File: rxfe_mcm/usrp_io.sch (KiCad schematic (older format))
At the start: 17 parts, among them J201 DB15, U202 CONN_SMA, U203 74HC04_FULL, U204 CONN_SMA, U205 ADP7158, U206 CONN_SMA, U209 CONN_SMA

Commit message: added some notes/errata to the transmitter schematics
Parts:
- J201: PN (none) -> 609-1498-ND
- RP201, RP202, RP204: PN (none) -> TC164J-1.0KCT-ND
- U202, U204, U206, U209: PN (none) -> CONSMA002-L-ND
- U203: PN (none) -> 296-8208-1-ND
- U205: PN (none) -> ADP7158ACPZ-3.3-R7CT-ND
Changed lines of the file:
@@
 LIBS:adp7158
 LIBS:pe4312
+LIBS:rxfe_mcm-cache
 EELAYER 25 0
 EELAYER END
@@
 F 2 "footprints:DB15MC" H 1700 1750 50  0001 C CNN
 F 3 "" H 1700 1750 50  0000 C CNN
+F 4 "609-1498-ND" H 1700 1750 60  0001 C CNN "PN"
 	1    1700 1750
 	-1   0    0    -1
@@
 F 2 "footprints:SMA_rightangle" H 1750 6800 60  0001 C CNN
 F 3 "" H 1750 6800 60  0000 C CNN
+F 4 "CONSMA002-L-ND" H 1750 6800 60  0001 C CNN "PN"
 	1    1750 6800
 	-1   0    0    -1
@@
 F 2 "Resistors_SMD:R_Array_Concave_4x0603" H 3550 2150 50  0001 C CNN
 F 3 "" H 3550 2150 50  0000 C CNN
+F 4 "TC164J-1.0KCT-ND" H 3550 2150 60  0001 C CNN "PN"
 	1    3550 2150
 	1    0    0    1
@@
 F 2 "Resistors_SMD:R_Array_Concave_4x0603" H 3550 1000 50  0001 C CNN
 F 3 "" H 3550 1000 50  0000 C CNN
+F 4 "TC164J-1.0KCT-ND" H 3550 1000 60  0001 C CNN "PN"
 	1    3550 1000
 	1    0    0    1
@@
 F 2 "Housings_SSOP:TSSOP-14_4.4x5mm_Pitch0.65mm" H 8100 2300 60  0001 C CNN
 F 3 "" H 8100 2300 60  0000 C CNN
+F 4 "296-8208-1-ND" H 8100 2300 60  0001 C CNN "PN"
 	1    8100 2300
 	1    0    0    -1
@@
 $EndComp
 $Comp
-L GND #PWR03
+L GND #PWR01
 U 1 1 59826F34
 P 9000 1750
-F 0 "#PWR03" H 9000 1500 50  0001 C CNN
+F 0 "#PWR01" H 9000 1500 50  0001 C CNN
 F 1 "GND" H 9000 1600 50  0000 C CNN
 F 2 "" H 9000 1750 50  0000 C CNN
@@
 AMPB2_CTRL
 $Comp
-L GND #PWR04
+L GND #PWR02
 U 1 1 5982BDE0
 P 7550 2700
-F 0 "#PWR04" H 7550 2450 50  0001 C CNN
+F 0 "#PWR02" H 7550 2450 50  0001 C CNN
 F 1 "GND" H 7550 2550 50  0000 C CNN
 F 2 "" H 7550 2700 50  0000 C CNN
@@
 F 2 "Housings_DFN_QFN:DFN-10-1EP_3x3mm_Pitch0.5mm" H 8150 4550 60  0001 C CNN
 F 3 "" H 8150 4550 60  0001 C CNN
+F 4 "ADP7158ACPZ-3.3-R7CT-ND" H 8150 4550 60  0001 C CNN "PN"
 	1    8150 4550
 	1    0    0    -1
@@
 $EndComp
 $Comp
-L GND #PWR05
+L GND #PWR03
 U 1 1 598D7D01
 P 9400 1750
-F 0 "#PWR05" H 9400 1500 50  0001 C CNN
+F 0 "#PWR03" H 9400 1500 50  0001 C CNN
 F 1 "GND" H 9400 1600 50  0000 C CNN
 F 2 "" H 9400 1750 50  0000 C CNN
@@
 $EndComp
 $Comp
-L +3V3 #PWR06
+L +3V3 #PWR04
 U 1 1 598DD83D
 P 7000 4200
-F 0 "#PWR06" H 7000 4050 50  0001 C CNN
+F 0 "#PWR04" H 7000 4050 50  0001 C CNN
 F 1 "+3V3" H 7000 4340 50  0000 C CNN
 F 2 "" H 7000 4200 50  0000 C CNN
@@
 $EndComp
 $Comp
-L VPP #PWR07
+L VPP #PWR05
 U 1 1 59903DFA
 P 9700 4200
-F 0 "#PWR07" H 9700 4050 50  0001 C CNN
+F 0 "#PWR05" H 9700 4050 50  0001 C CNN
 F 1 "VPP" H 9700 4350 50  0000 C CNN
 F 2 "" H 9700 4200 50  0000 C CNN
@@
 $EndComp
 $Comp
-L GND #PWR08
+L GND #PWR06
 U 1 1 599045BA
 P 8900 5300
-F 0 "#PWR08" H 8900 5050 50  0001 C CNN
+F 0 "#PWR06" H 8900 5050 50  0001 C CNN
 F 1 "GND" H 8900 5150 50  0000 C CNN
 F 2 "" H 8900 5300 50  0000 C CNN
@@
 $EndComp
 $Comp
-L GND #PWR09
+L GND #PWR07
 U 1 1 59904683
 P 9300 5300
-F 0 "#PWR09" H 9300 5050 50  0001 C CNN
+F 0 "#PWR07" H 9300 5050 50  0001 C CNN
 F 1 "GND" H 9300 5150 50  0000 C CNN
 F 2 "" H 9300 5300 50  0000 C CNN
@@
 $EndComp
 $Comp
-L GND #PWR010
+L GND #PWR08
 U 1 1 599046FD
 P 9700 5300
-F 0 "#PWR010" H 9700 5050 50  0001 C CNN
+F 0 "#PWR08" H 9700 5050 50  0001 C CNN
 F 1 "GND" H 9700 5150 50  0000 C CNN
 F 2 "" H 9700 5300 50  0000 C CNN
@@
 $EndComp
 $Comp
-L GND #PWR011
+L GND #PWR09
 U 1 1 599050DD
 P 7300 5300
-F 0 "#PWR011" H 7300 5050 50  0001 C CNN
+F 0 "#PWR09" H 7300 5050 50  0001 C CNN
 F 1 "GND" H 7300 5150 50  0000 C CNN
 F 2 "" H 7300 5300 50  0000 C CNN
@@
 $EndComp
 $Comp
-L GND #PWR012
+L GND #PWR010
 U 1 1 5990515D
 P 7000 5300
-F 0 "#PWR012" H 7000 5050 50  0001 C CNN
+F 0 "#PWR010" H 7000 5050 50  0001 C CNN
 F 1 "GND" H 7000 5150 50  0000 C CNN
 F 2 "" H 7000 5300 50  0000 C CNN
@@
 $EndComp
 $Comp
-L GND #PWR013
+L GND #PWR011
 U 1 1 59905965
 P 8150 5300
-F 0 "#PWR013" H 8150 5050 50  0001 C CNN
+F 0 "#PWR011" H 8150 5050 50  0001 C CNN
 F 1 "GND" H 8150 5150 50  0000 C CNN
 F 2 "" H 8150 5300 50  0000 C CNN
@@
 $EndComp
 $Comp
-L VPP #PWR014
+L VPP #PWR012
 U 1 1 5990693F
 P 7500 5100
-F 0 "#PWR014" H 7500 4950 50  0001 C CNN
+F 0 "#PWR012" H 7500 4950 50  0001 C CNN
 F 1 "VPP" H 7500 5250 50  0000 C CNN
 F 2 "" H 7500 5100 50  0000 C CNN
@@
 $EndComp
 $Comp
-L +3V3 #PWR015
+L +3V3 #PWR013
 U 1 1 5991D035
 P 9000 1050
-F 0 "#PWR015" H 9000 900 50  0001 C CNN
+F 0 "#PWR013" H 9000 900 50  0001 C CNN
 F 1 "+3V3" H 9000 1190 50  0000 C CNN
 F 2 "" H 9000 1050 50  0000 C CNN
@@
 $EndComp
 $Comp
-L GND #PWR016
+L GND #PWR014
 U 1 1 5983E2EE
 P 1800 7450
-F 0 "#PWR016" H 1800 7200 50  0001 C CNN
+F 0 "#PWR014" H 1800 7200 50  0001 C CNN
 F 1 "GND" H 1800 7300 50  0000 C CNN
 F 2 "" H 1800 7450 50  0000 C CNN
@@
 F 2 "footprints:SMA_rightangle" H 1750 5600 60  0001 C CNN
 F 3 "" H 1750 5600 60  0000 C CNN
+F 4 "CONSMA002-L-ND" H 1750 5600 60  0001 C CNN "PN"
 	1    1750 5600
 	-1   0    0    -1
 $EndComp
 $Comp
-L GND #PWR017
+L GND #PWR015
 U 1 1 5983EAFB
 P 1800 6250
-F 0 "#PWR017" H 1800 6000 50  0001 C CNN
+F 0 "#PWR015" H 1800 6000 50  0001 C CNN
 F 1 "GND" H 1800 6100 50  0000 C CNN
 F 2 "" H 1800 6250 50  0000 C CNN
@@
 F 2 "footprints:SMA_rightangle" H 1750 4200 60  0001 C CNN
 F 3 "" H 1750 4200 60  0000 C CNN
+F 4 "CONSMA002-L-ND" H 1750 4200 60  0001 C CNN "PN"
 	1    1750 4200
 	-1   0    0    -1
 $EndComp
 $Comp
-L GND #PWR018
+L GND #PWR016
 U 1 1 5983ED3F
 P 1800 4850
-F 0 "#PWR018" H 1800 4600 50  0001 C CNN
+F 0 "#PWR016" H 1800 4600 50  0001 C CNN
 F 1 "GND" H 1800 4700 50  0000 C CNN
 F 2 "" H 1800 4850 50  0000 C CNN
@@
 F 2 "footprints:SMA_rightangle" H 1750 3000 60  0001 C CNN
 F 3 "" H 1750 3000 60  0000 C CNN
+F 4 "CONSMA002-L-ND" H 1750 3000 60  0001 C CNN "PN"
 	1    1750 3000
 	-1   0    0    -1
 $EndComp
 $Comp
-L GND #PWR019
+L GND #PWR017
 U 1 1 5983ED56
 P 1800 3650
-F 0 "#PWR019" H 1800 3400 50  0001 C CNN
+F 0 "#PWR017" H 1800 3400 50  0001 C CNN
 F 1 "GND" H 1800 3500 50  0000 C CNN
 F 2 "" H 1800 3650 50  0000 C CNN
@@
 F 2 "Resistors_SMD:R_Array_Concave_4x0603" H 3550 1600 50  0001 C CNN
 F 3 "" H 3550 1600 50  0000 C CNN
+F 4 "TC164J-1.0KCT-ND" H 3550 1600 60  0001 C CNN "PN"
 	1    3550 1600
 	1    0    0    1
@@
 TODO: add IO header\n
 $Comp
-L GND #PWR?
+L GND #PWR018
 U 1 1 5986664A
 P 2250 1350
-F 0 "#PWR?" H 2250 1100 50  0001 C CNN
+F 0 "#PWR018" H 2250 1100 50  0001 C CNN
 F 1 "GND" H 2250 1200 50  0000 C CNN
 F 2 "" H 2250 1350 50  0000 C CNN
@@
 $EndComp
 $Comp
-L GND #PWR?
+L GND #PWR019
 U 1 1 598666AA
 P 2250 1150
-F 0 "#PWR?" H 2250 900 50  0001 C CNN
+F 0 "#PWR019" H 2250 900 50  0001 C CNN
 F 1 "GND" H 2250 1000 50  0000 C CNN
 F 2 "" H 2250 1150 50  0000 C CNN

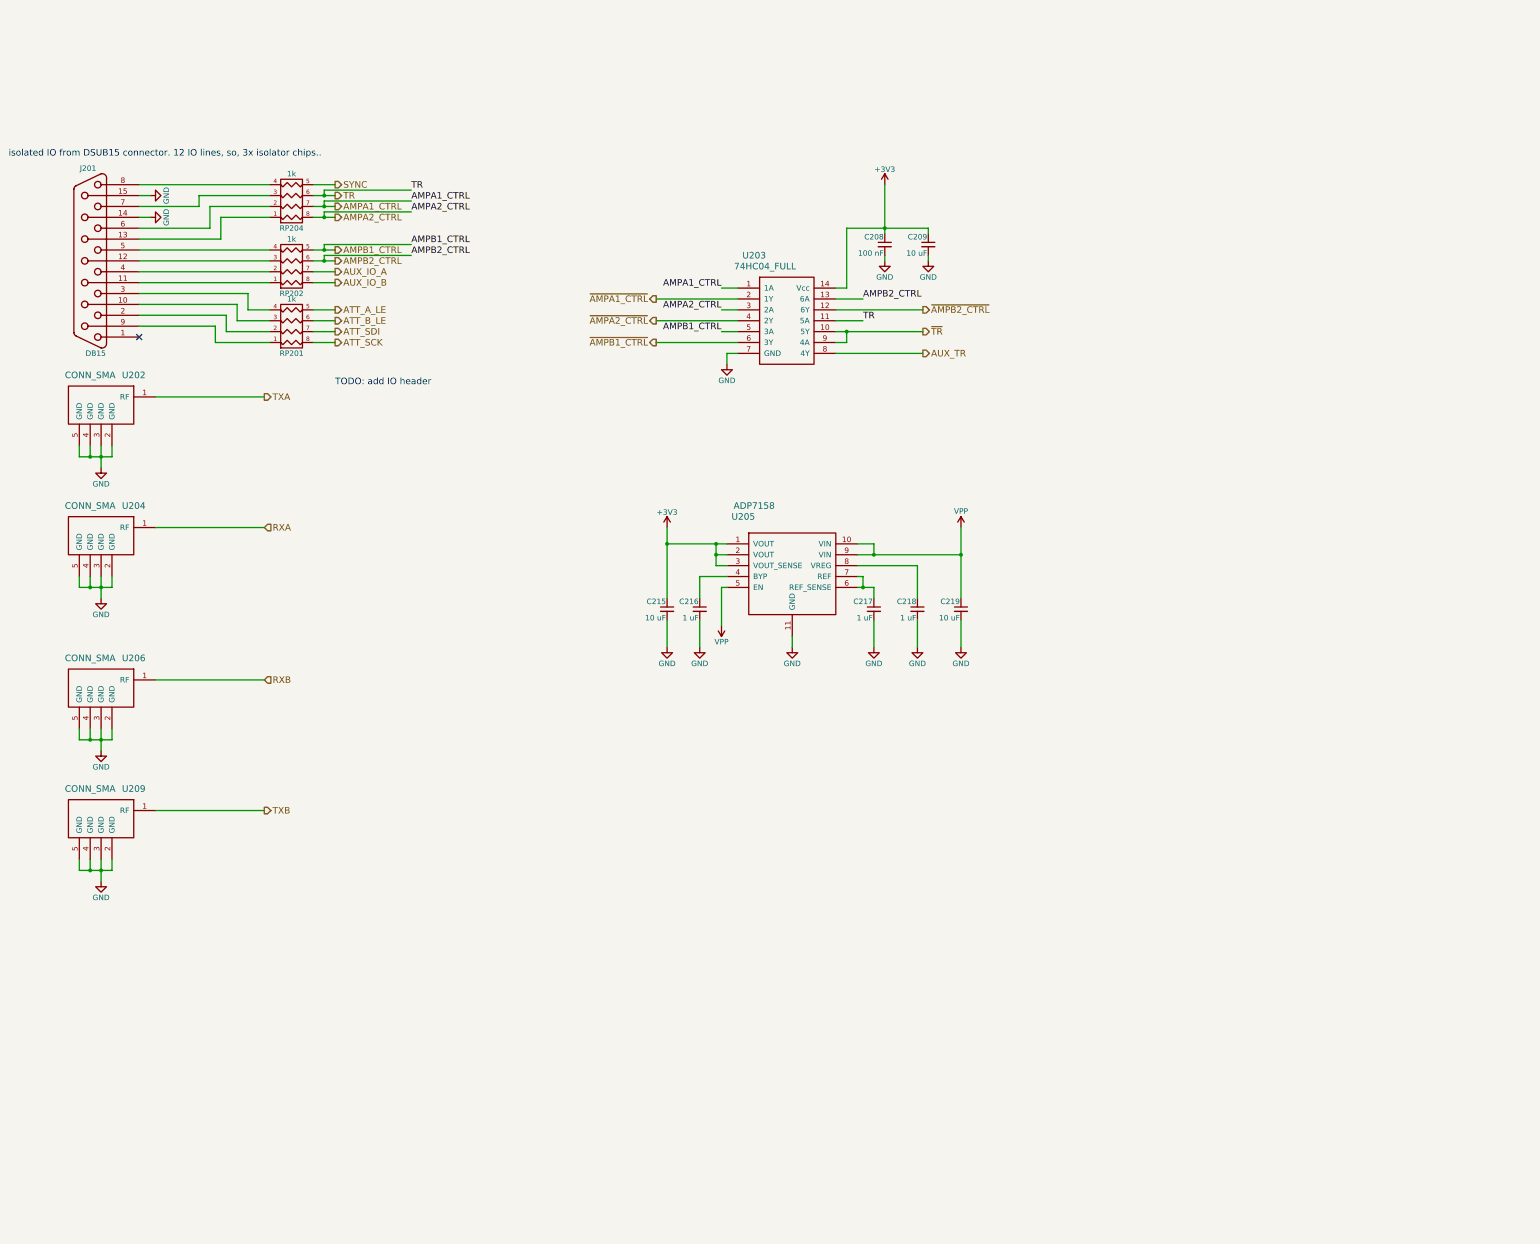
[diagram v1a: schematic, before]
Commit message: added tvs diodes to external connections on mcm_rxfe
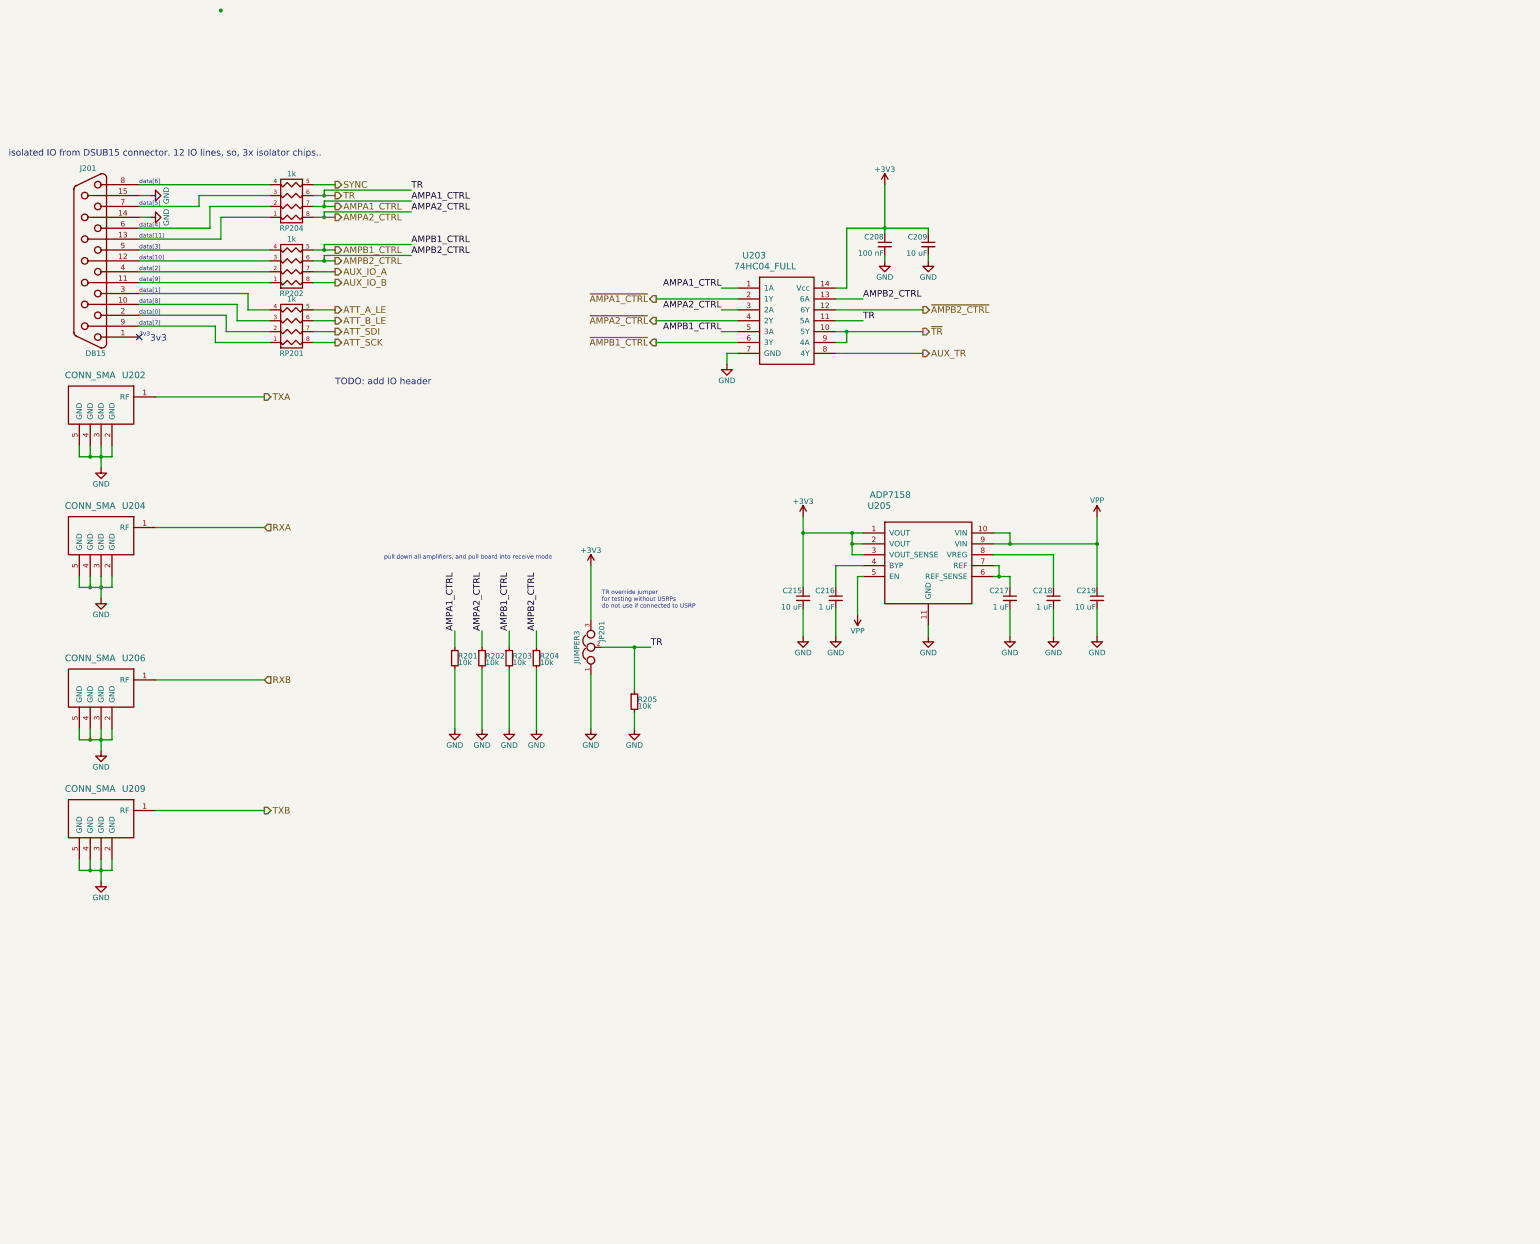
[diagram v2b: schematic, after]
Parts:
- added JP201: JUMPER3, Pin_Headers:Pin_Header_Straight_1x03, symbol JUMPER3
- added R201, R202, R203, R204, R205: 10k, Resistors_SMD:R_0603, symbol R_Small
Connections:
- net +3V3: now also JP201.3
- net AMPA1_CTRL: now also R201.1
- net AMPA2_CTRL: now also R202.1
- net AMPB1_CTRL: now also R203.1
- net AMPB2_CTRL: now also R204.1
- net GND: now also JP201.1, R201.2, R202.2, R203.2, R204.2, R205.2
- net TR: now also JP201.2, R205.1
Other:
- note added: "3v3"
- note added: "TR override jumper\nfor testing without USRPs\ndo not use if connected to USRP"
- note added: "data[0]"
- note added: "data[10]"
- note added: "data[11]"
- note added: "data[1]"
- note added: "data[2]"
- note added: "data[3]"
- note added: "data[4]"
- note added: "data[5]"
- note added: "data[6]"
- note added: "data[7]"
- note added: "data[8]"
- note added: "data[9]"
- note added: "pull down all amplifiers, and pull board into receive mode"
- moved on the sheet: C215, C216, C217, C218, C219, U205

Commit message: add input protection to mcm usrp front end, modified to also work at kodiak
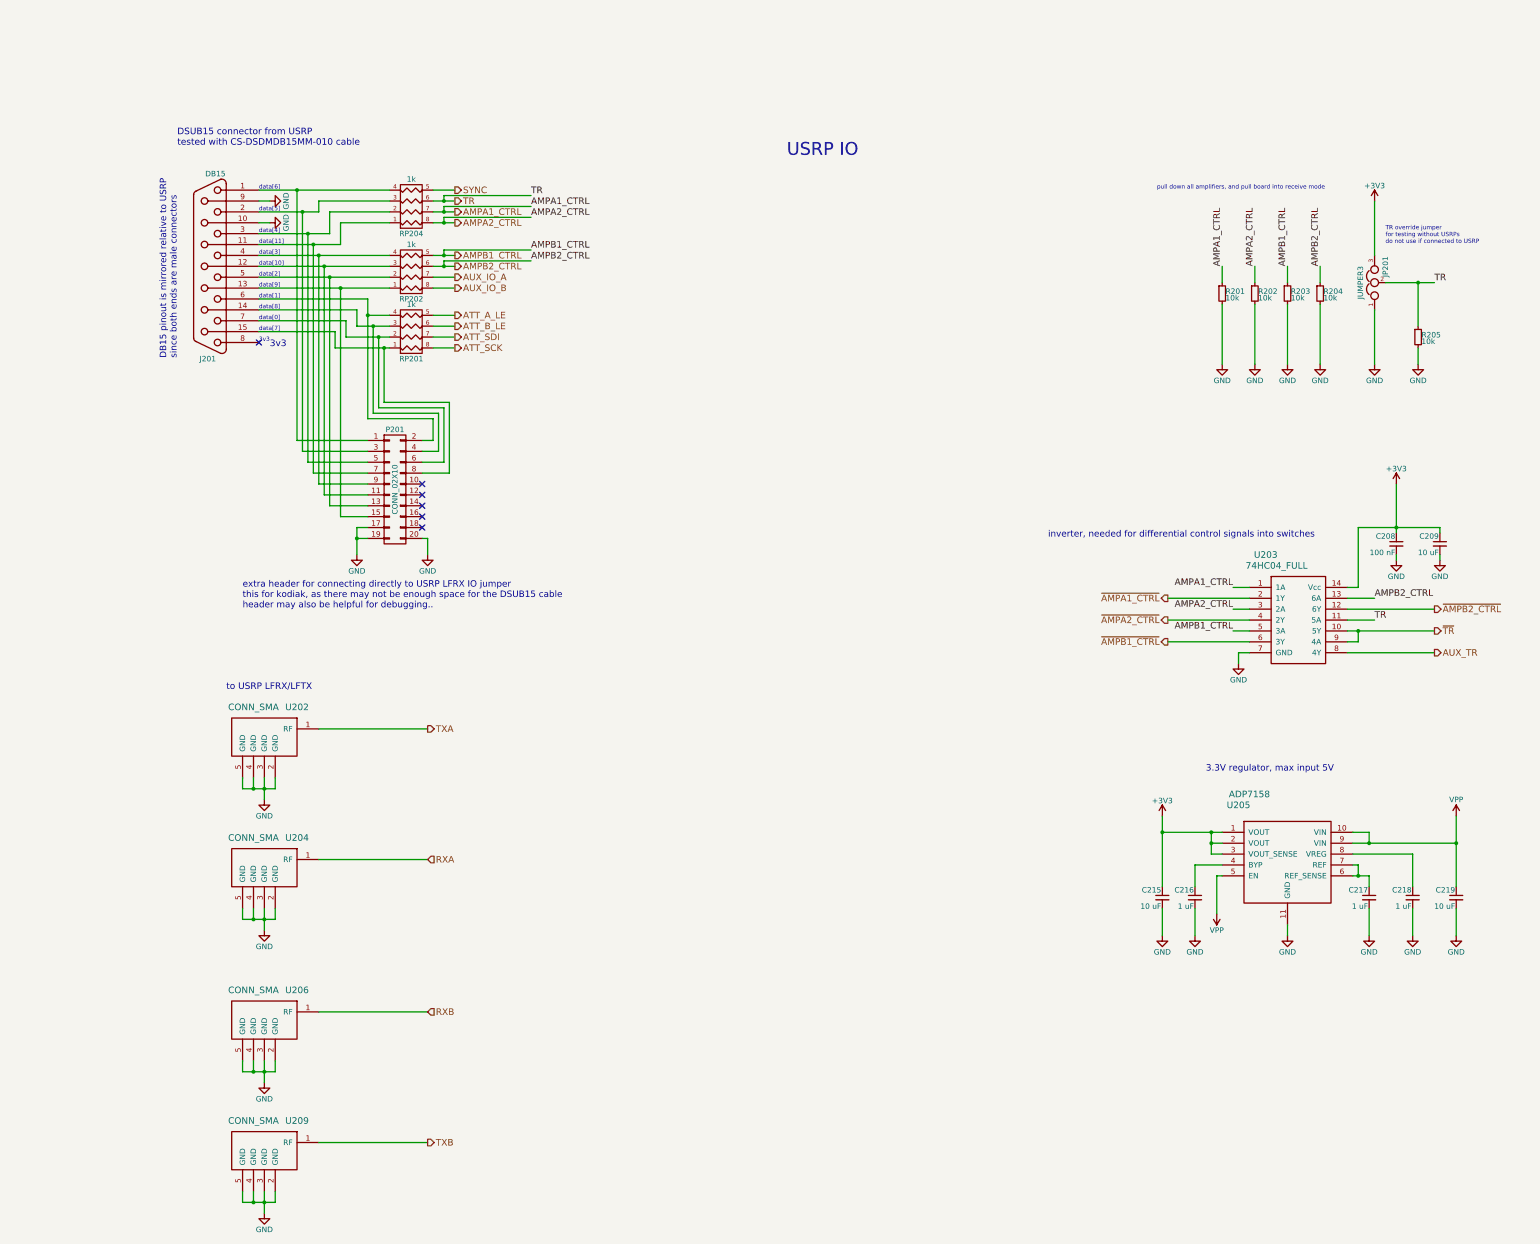
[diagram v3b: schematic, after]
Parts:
- added P201: CONN_02X10, Pin_Headers:Pin_Header_Straight_2x10, symbol CONN_02X10
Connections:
- net GND: now also J201.10 (P10), J201.9 (P9), P201.17 (P17), P201.19 (P19), P201.20 (P20); no longer J201.14 (P14), J201.15 (P15)
- net at J201.1: now also RP204.4 (P4), P201.1 (P1)
- net at RP201.3 (P3): now also J201.14 (P14), P201.4 (P4); no longer J201.10 (P10)
- net at J201.11 (P111): now also RP204.1 (P1), P201.7 (P7); no longer RP202.1 (P1)
- net at J201.12 (P12), RP202.3 (P3): now also P201.11 (P11)
- net at J201.13 (P13): now also RP202.1 (P1), P201.15 (P15); no longer RP204.1 (P1)
- net at J201.2: now also RP204.3 (P3), P201.3 (P3); no longer RP201.2 (P2)
- net at J201.3: now also RP204.2 (P2), P201.5 (P5); no longer RP201.4 (P4)
- net at J201.4: now also RP202.4 (P4), P201.9 (P9); no longer RP202.2 (P2)
- net at J201.5: now also RP202.2 (P2), P201.13 (P13); no longer RP202.4 (P4)
- net at J201.6: now also RP201.4 (P4), P201.2 (P2); no longer RP204.2 (P2)
- net at J201.7: now also RP201.2 (P2), P201.6 (P6); no longer RP204.3 (P3)
- net at J201.8: no longer RP204.4 (P4)
- net at RP201.1 (P1): now also J201.15 (P15), P201.8 (P8); no longer J201.9 (P9)
- no-connect marks 1 -> 6
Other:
- note added: "3.3V regulator, max input 5V"
- note added: "DB15 pinout is mirrored relative to USRP\nsince both ends are male connectors"
- note added: "DSUB15 connector from USRP\ntested with CS-DSDMDB15MM-010 cable"
- note added: "USRP IO"
- note added: "extra header for connecting directly to USRP LFRX IO jumper\nthis for kodiak, as there may not be enough space for the DSUB15 cable\nheader may also be helpful for debugging.."
- note added: "inverter, needed for differential control signals into switches"
- note added: "to USRP LFRX/LFTX"
- note removed: "TODO: add IO header\n"
- note removed: "isolated IO from DSUB15 connector. 12 IO lines, so, 3x isolator chips.."
- moved on the sheet: C208, C209, C215, C216, C217, C218, C219, J201, JP201, R201, R202, R203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

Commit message: a bit of work on layout..
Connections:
- net at J201.1, RP204.4 (P4): now also P201.12 (P12); no longer P201.1 (P1)
- net at J201.11 (P111), RP204.1 (P1): now also P201.9 (P9); no longer P201.7 (P7)
- net at J201.12 (P12), RP202.3 (P3): now also P201.7 (P7); no longer P201.11 (P11)
- net at J201.13 (P13), RP202.1 (P1): now also P201.5 (P5); no longer P201.15 (P15)
- net at J201.14 (P14), RP201.3 (P3): now also P201.3 (P3); no longer P201.4 (P4)
- net at J201.15 (P15), RP201.1 (P1): now also P201.1 (P1); no longer P201.8 (P8)
- net at J201.2, RP204.3 (P3): now also P201.11 (P11); no longer P201.3 (P3)
- net at J201.3, RP204.2 (P2): now also P201.10 (P10); no longer P201.5 (P5)
- net at J201.4, RP202.4 (P4): now also P201.8 (P8); no longer P201.9 (P9)
- net at J201.5, RP202.2 (P2): now also P201.6 (P6); no longer P201.13 (P13)
- net at J201.6, RP201.4 (P4): now also P201.4 (P4); no longer P201.2 (P2)
- net at J201.7, RP201.2 (P2): now also P201.2 (P2); no longer P201.6 (P6)
- no-connect marks 6 -> 1
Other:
- note added: "TODO: use net names instead of wiring.. this is messy"
- moved on the sheet: P201
